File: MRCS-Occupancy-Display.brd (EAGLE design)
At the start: 106 x 100 mm, 4 parts

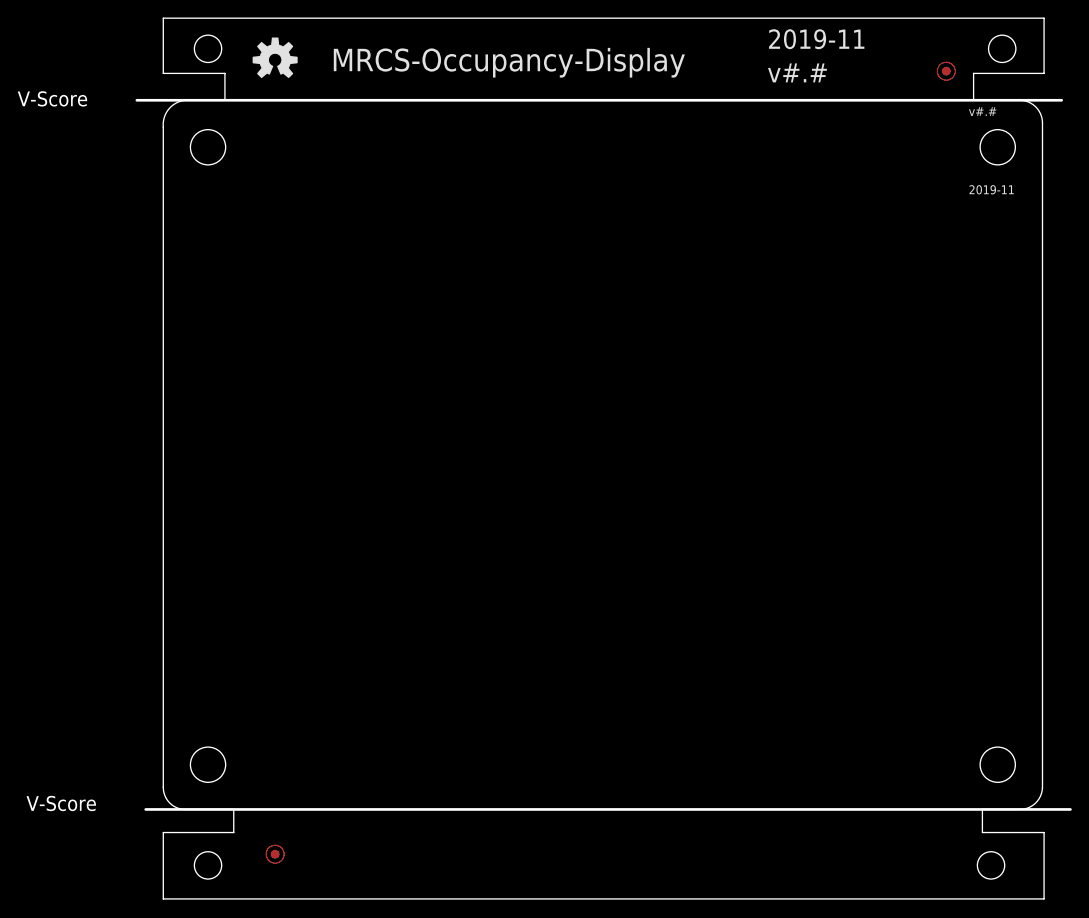
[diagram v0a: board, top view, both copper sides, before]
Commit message: first pass of V1.0
basic 5x7 CM board per Allison
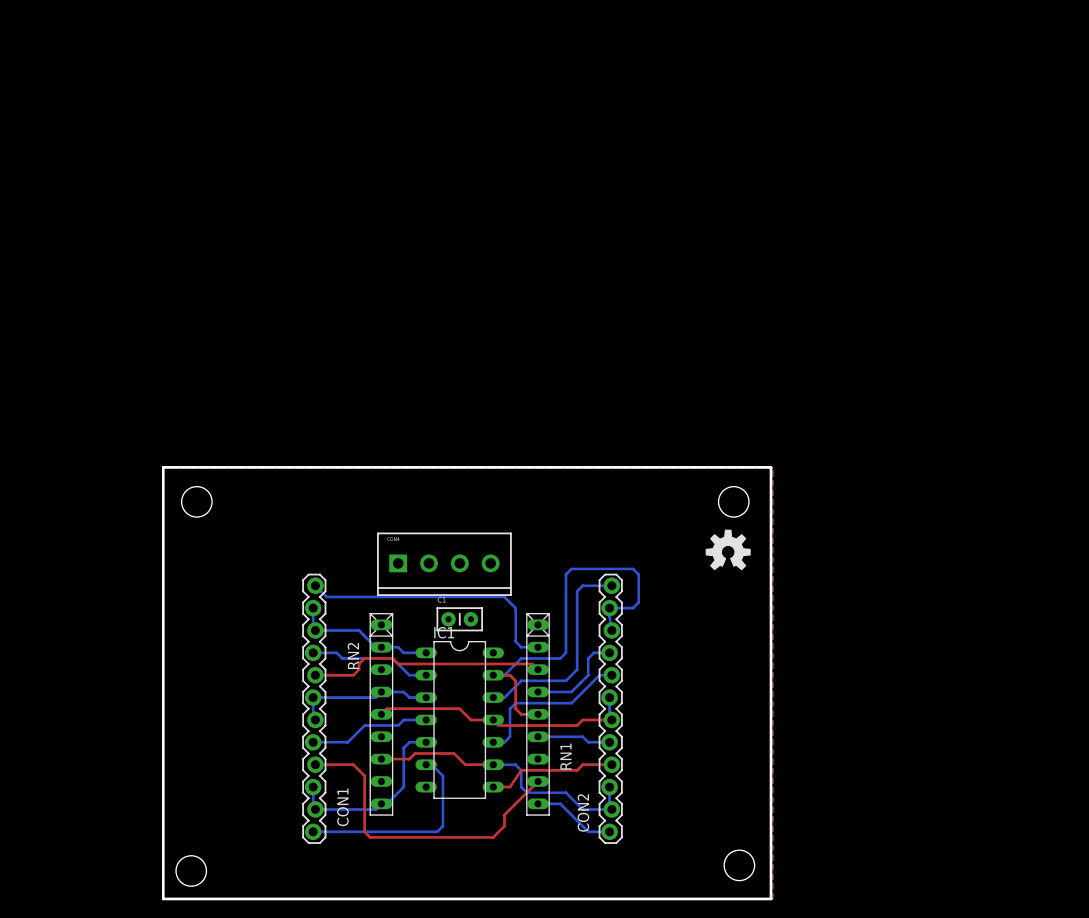
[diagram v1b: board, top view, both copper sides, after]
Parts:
- removed BOARD1: BOARD80X100, SPCoast:BOARD-DINRAIL-3.17INX10CM
- removed FID1, FID2: FIDUCIAL, SPCoast:FIDUCIAL_1MM
- added C1: 0.1 uF, SPCoast:C-PTH-0.100
- added CON1, CON2: CONNECTOR-M12LOCK, SPCoast:1X12_LOCK
- added CON4: (no value), SPCoast:SCREWTERMINAL-3.5MM-4
- added IC1: 74ALS04N, 74xx-us:DIL14
- added RN1: 470, resistor-net:RN-9
- added RN2: 4.7K, resistor-net:RN-9
- added U$1: (no value), MRCS-prop65warningBtm:CA-PROP65WARNING
- added U$2: (no value), MRCSLogoBtm:MRCSLOGOBTM
- moved OSHW1 75.9 mm to (64.1, 39.4)
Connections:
- new net GND: C1.2, CON4.1, CON4.3, IC1.7
- new net N$1: CON1.2, CON1.3, IC1.1, RN2.2
- new net N$10: CON1.9, RN1.8
- new net N$11: CON2.8, IC1.10
- new net N$12: CON2.12, IC1.12
- new net N$13: CON2.4, IC1.8
- new net N$14: CON2.1, RN1.9
- new net N$15: CON2.5, RN1.6
- new net N$18: CON2.6, CON2.7, IC1.11, RN2.5
- new net N$19: CON2.9, RN1.4
- new net N$2: CON1.10, CON1.11, IC1.5, RN2.9
- new net N$20: CON2.10, CON2.11, IC1.13, RN1.5
- new net N$3: CON1.1, RN1.2
- new net N$4: CON1.4, IC1.2
- new net N$5: CON1.6, CON1.7, IC1.3, RN2.4
- new net N$6: CON1.12, IC1.6
- new net N$7: CON1.8, IC1.4
- new net N$8: CON1.5, RN1.3
- new net N$9: CON2.2, CON2.3, IC1.9, RN2.7
- new net VCC: C1.1, CON4.2, CON4.4, IC1.14, RN1.1, RN2.1
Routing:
- net N$20: track 0.00 -> 45.1 mm
- net N$10: track 0.00 -> 35.8 mm
- net N$9: track 0.00 -> 32.8 mm
- net N$3: track 0.00 -> 30.4 mm
- net N$18: track 0.00 -> 30.1 mm
- net N$8: track 0.00 -> 27.0 mm
- net N$12: track 0.00 -> 23.9 mm
- net N$6: track 0.00 -> 23.1 mm
- net N$2: track 0.00 -> 21.0 mm
- net N$11: track 0.00 -> 18.5 mm
- net N$1: track 0.00 -> 16.3 mm
- net N$5: track 0.00 -> 15.9 mm
- net N$4: track 0.00 -> 15.1 mm
- net N$13: track 0.00 -> 14.7 mm
- net N$7: track 0.00 -> 13.9 mm
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- added copper zone on layer 16, net GND
- added copper zone on layer 1, net VCC
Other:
- board size 106 x 100 mm -> 69 x 49 mm
- board text added: "BiPolar LED Occupancy"
- board text added: "CROG ARDN"
- board text added: "G 5 G 5"
- board text added: "Seth Neumann Allison Dendy"
- board text added: "V 1.0 20230920"
- board text removed: "2019-11"
- board text removed: ">DRAWING_NAME"
- board text removed: "Use tPlace/bPlace for silkscreen text and drawings Use Document, tDocu and bDocu for assembly notes and documentation that does NOT go on the board"
- board text removed: "v#.#"

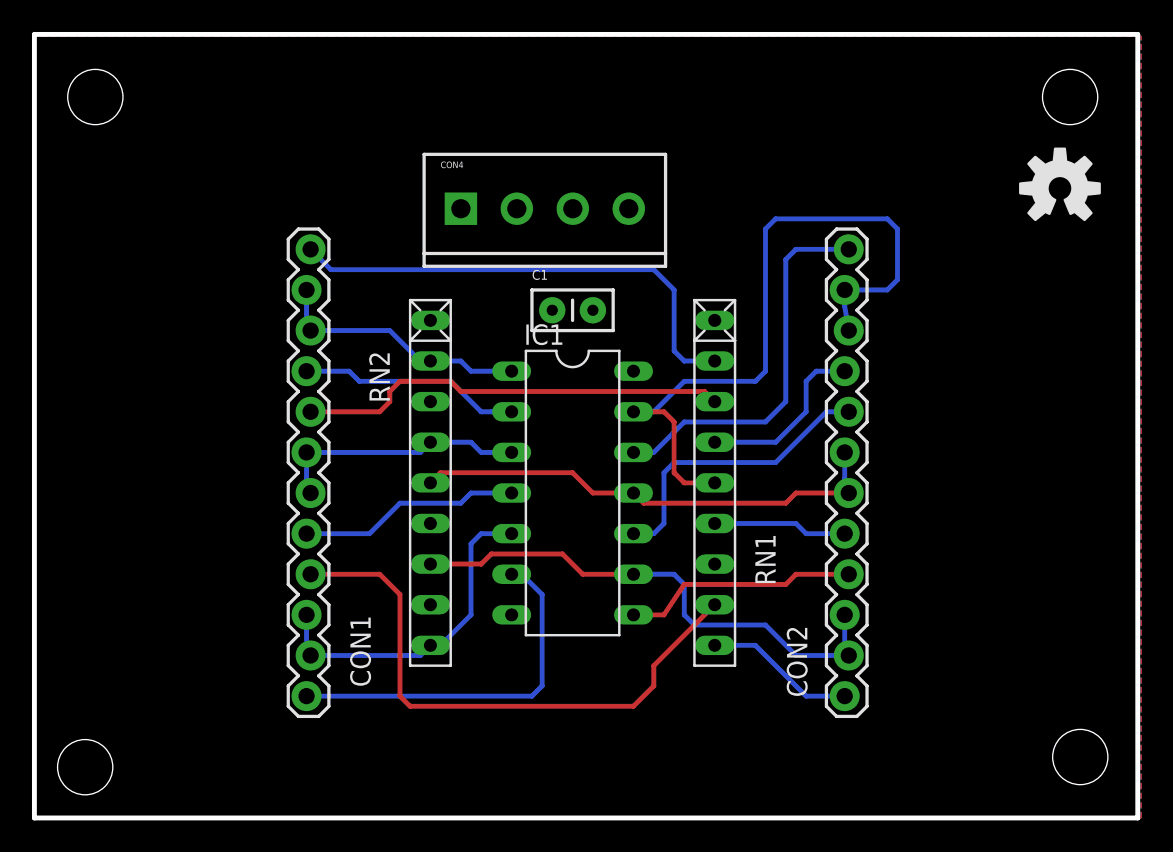
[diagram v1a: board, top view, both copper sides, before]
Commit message: modified the base design from 5x7 to 5x5 CM
The intent is to make a smaller footprint for panelization. It's pretty tight and not much room for labels.
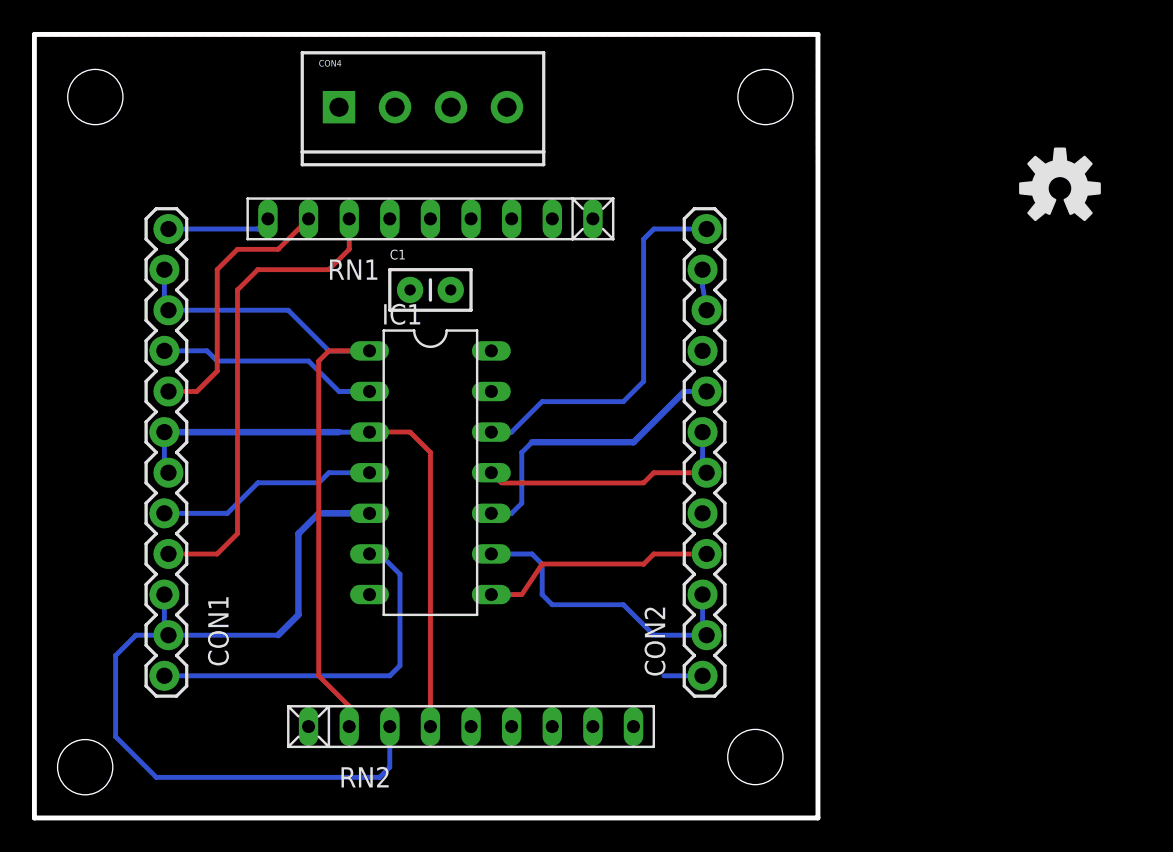
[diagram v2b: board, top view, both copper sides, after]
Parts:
- moved RN1 24.3 mm to (24.8, 37.5), turned to 180 degrees
- moved RN2 15.5 mm to (27.3, 5.71), turned to 0 degrees
- moved CON4 9.92 mm to (19.1, 44.5)
- moved C1 8.98 mm to (24.8, 33.0)
- moved CON2 8.98 mm to (41.9, 8.89)
- moved IC1 8.98 mm to (24.8, 21.6)
- moved CON1 8.98 mm to (8.26, 36.8)
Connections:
- net N$10: now also RN1.7; no longer RN1.8
- net N$14: now also RN1.2; no longer RN1.9
- net N$2: now also RN2.3; no longer RN2.9
- net N$3: now also RN1.9; no longer RN1.2
- net N$8: now also RN1.8; no longer RN1.3
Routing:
- net N$20: track 45.1 -> 2.56 mm
- net N$2: track 21.0 -> 51.3 mm
- net N$1: track 16.3 -> 43.4 mm
- net N$3: track 30.4 -> 6.49 mm
- net N$5: track 15.9 -> 36.9 mm
- net N$18: track 30.1 -> 16.6 mm
- net N$9: track 32.8 -> 19.3 mm
- net N$19: track 11.1 -> 0.00 mm
- net N$8: track 27.0 -> 17.0 mm
- net N$15: track 8.39 -> 0.00 mm
- net N$14: track 9.44 -> 2.41 mm
- net N$10: track 35.8 -> 30.0 mm
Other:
- board size 69 x 49 mm -> 49 x 49 mm

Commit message: cleanup prior to putting product up on website
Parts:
- added C2: 0.1 uF, SPCoast:C050-024X044
- added LED1: (no value), SPCoast:LED3MM
- moved OSHW1 55.0 mm to (9.53, 45.7)
- moved U$2 53.5 mm to (7.62, 41.9)
- moved U$1 19.3 mm to (45.1, 25.4), turned to 90 degrees
- moved RN2 4.02 mm to (23.5, 4.45)
- moved CON2 3.81 mm to (38.1, 8.89)
- moved C1 2.84 mm to (23.5, 30.5)
- moved IC1 2.84 mm to (23.5, 19.1)
- moved RN1 2.84 mm to (23.5, 40.0)
- moved CON1 1.90 mm to (10.2, 36.8)
- moved CON4 1.80 mm to (17.8, 45.7)
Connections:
- removed net N$1: CON1.2, CON1.3, IC1.1, RN2.2
- new net N$16: CON1.2, CON1.3, IC1.1, RN2.3
- new net N$17: LED1.A, RN1.5
- net GND: now also C2.2, LED1.K
- net N$15: now also RN1.4; no longer RN1.6
- net N$18: now also RN2.7; no longer RN2.5
- net N$19: now also RN1.3; no longer RN1.4
- net N$2: now also RN2.2; no longer RN2.3
- net N$20: now also RN2.6; no longer RN1.5
- net N$9: now also RN2.9; no longer RN2.7
- net VCC: now also C2.1
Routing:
- net N$14: track 2.41 -> 55.4 mm
- net N$1: track 43.4 -> 0.00 mm
- net N$15: track 0.00 -> 41.4 mm
- net N$16: track 0.00 -> 39.2 mm
- net N$20: track 2.56 -> 39.0 mm
- net N$19: track 0.00 -> 26.9 mm
- net N$2: track 51.3 -> 31.9 mm
- net N$18: track 16.6 -> 31.3 mm
- net N$6: track 23.1 -> 13.5 mm
- net N$5: track 36.9 -> 30.6 mm
- net N$9: track 19.3 -> 23.7 mm
- net N$7: track 13.9 -> 9.65 mm
- net N$17: track 0.00 -> 3.81 mm
- net N$4: track 15.1 -> 13.2 mm
- net N$8: track 17.0 -> 18.2 mm
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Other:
- board text added: "C1"
- board text added: "C2"
- board text added: "CON1"
- board text added: "CON2"
- board text added: "CON4"
- board text added: "CROG ADDN"
- board text added: "IC1"
- board text added: "LED1"
- board text added: "RN1"
- board text added: "RN2"
- board text added: "V 1.1 20231103"
- board text removed: "CROG ARDN"
- board text removed: "V 1.0 20230920"
